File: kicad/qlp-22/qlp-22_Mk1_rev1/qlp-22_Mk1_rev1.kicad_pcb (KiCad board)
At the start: 2 copper layers, 301 x 153 mm, 51 parts

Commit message: Adds row connections and diode/switch labels
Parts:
- added L0: MountingHole_2.2mm_M2, MountingHole:MountingHole_2.2mm_M2, F.Cu at (84.0, 149.0)
- added L1: MountingHole_2.2mm_M2, MountingHole:MountingHole_2.2mm_M2, F.Cu at (164.3, 162.3)
- added L2: MountingHole_2.2mm_M2, MountingHole:MountingHole_2.2mm_M2, F.Cu at (181.7, 231.4)
- added R3: MountingHole_2.2mm_M2, MountingHole:MountingHole_2.2mm_M2, F.Cu at (208.7, 231.4)
- added R4: MountingHole_2.2mm_M2, MountingHole:MountingHole_2.2mm_M2, F.Cu at (226.1, 162.3)
- moved R5 40.5 mm to (306.4, 149.0), turned to 20 degrees
- moved D1:11 18.3 mm to (333.6, 165.2)
- moved S1:1 18.3 mm to (79.9, 160.3)
- moved S1:11 18.3 mm to (329.3, 153.4)
- moved D1:4 18.3 mm to (135.4, 183.1)
- moved D1:1 18.3 mm to (75.6, 172.0)
- moved S1:6 18.3 mm to (230.2, 173.5)
- moved D1:0 18.3 mm to (56.8, 165.2)
- moved D0:8 18.3 mm to (254.1, 122.3)
- moved S0:11 18.3 mm to (245.6, 215.8)
- moved S1:4 18.3 mm to (139.7, 171.4)
- moved S0:10 18.3 mm to (228.5, 227.4)
- moved D1:3 18.3 mm to (120.0, 166.9)
- moved D0:7 18.3 mm to (238.7, 138.5)
- moved S1:9 18.3 mm to (286.6, 153.0)
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- renumbered REF** to D0:0, REF** to D0:1, REF** to D0:10, REF** to D0:11, REF** to D0:2, REF** to D0:3, REF** to D0:4, REF** to D0:7, REF** to D0:8, REF** to D0:9, REF** to D1:0, REF** to D1:1, REF** to D1:10, REF** to D1:11, REF** to D1:2, REF** to D1:3, REF** to D1:4, REF** to D1:5, REF** to D1:6, REF** to D1:7, REF** to D1:8, REF** to D1:9, REF** to R5, REF** to RESET, REF** to S0:0, REF** to S0:1, REF** to S0:10, REF** to S0:11, REF** to S0:2, REF** to S0:3, REF** to S0:4, REF** to S0:7, REF** to S0:8, REF** to S0:9, REF** to S1:0, REF** to S1:1, REF** to S1:10, REF** to S1:11, REF** to S1:2, REF** to S1:3, REF** to S1:4, REF** to S1:5, REF** to S1:6, REF** to S1:7, REF** to S1:8, REF** to S1:9
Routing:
- net (no net): track 4237.9 -> 4507.6 mm
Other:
- outline, holes or cut-outs redrawn
- board text added: "OLED 128x64"
- board text added: "Raspberry Pi Pico"

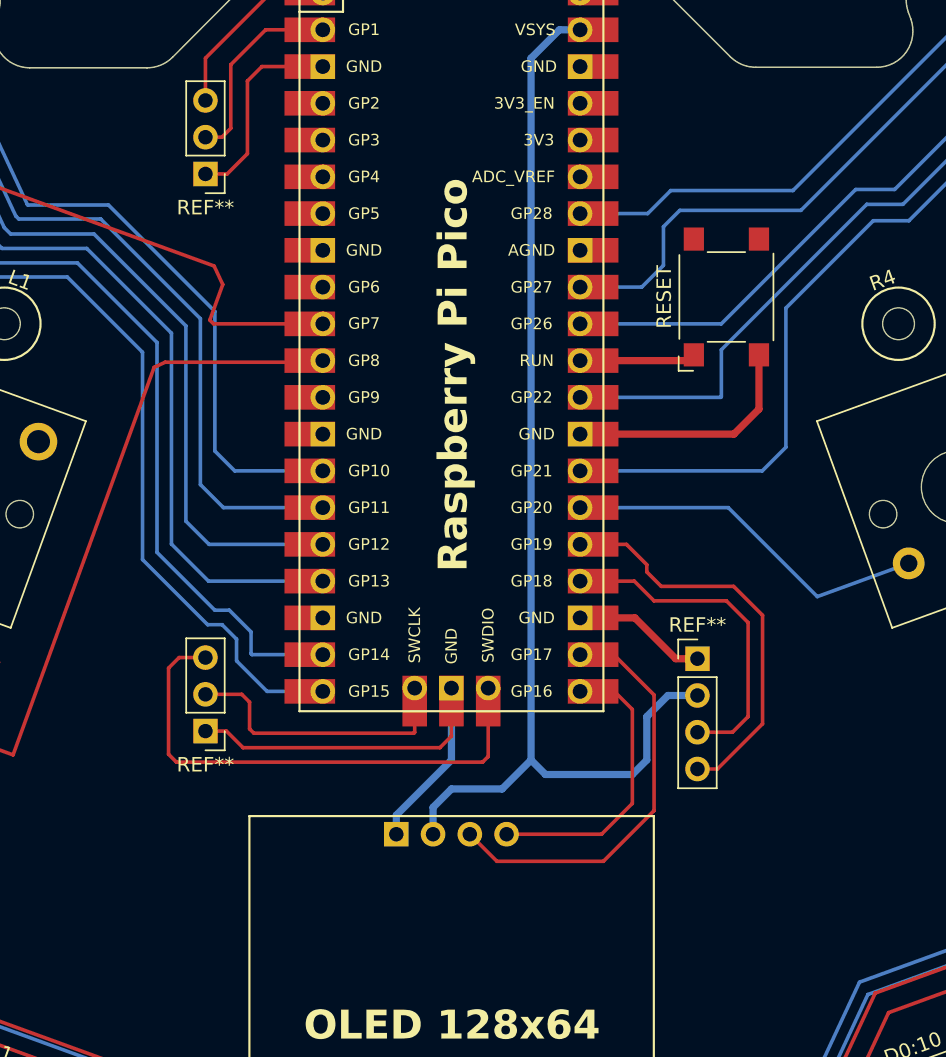
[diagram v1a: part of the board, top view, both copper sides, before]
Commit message: Adds pin labels for qlp-22_Mk1_rev1
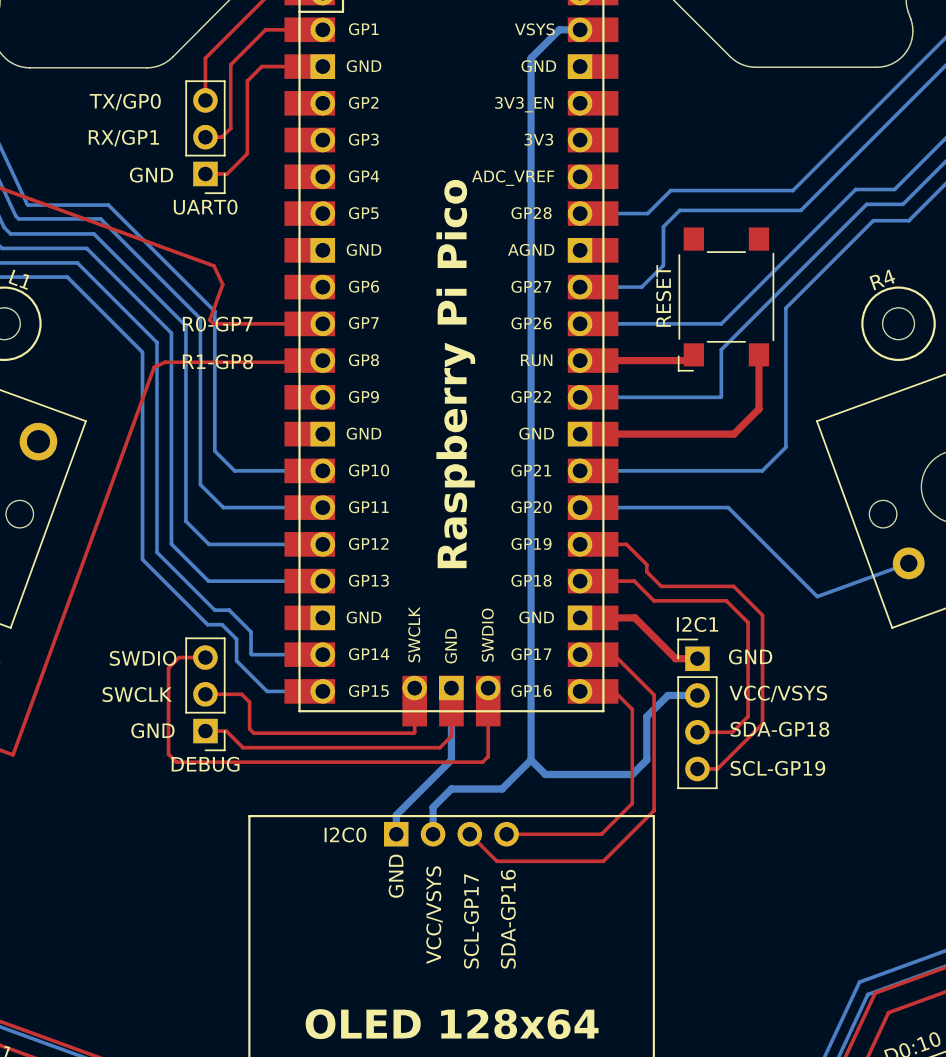
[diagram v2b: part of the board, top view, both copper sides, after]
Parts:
- renumbered REF** to DEBUG, REF** to I2C1, REF** to UART0
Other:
- board text added: "C0"
- board text added: "C1"
- board text added: "C10"
- board text added: "C11"
- board text added: "C2"
- board text added: "C3"
- board text added: "C4"
- board text added: "C5"
- board text added: "C6"
- board text added: "C7"
- board text added: "C8"
- board text added: "C9"
- board text added: "GND"
- board text added: "I2C0"
- board text added: "R0-GP7"
- board text added: "R1-GP8"
- board text added: "RX/GP1"
- board text added: "SCL-GP17"
- board text added: "SCL-GP19"
- board text added: "SDA-GP16"
- board text added: "SDA-GP18"
- board text added: "SWCLK"
- board text added: "SWDIO"
- board text added: "TX/GP0"
- board text added: "VCC/VSYS"
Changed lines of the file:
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@@
     (tags "Through hole pin header THT 1x04 2.54mm single row")
     (attr through_hole)
-    (fp_text reference "REF**" (at 0 -2.33) (layer "F.SilkS")
+    (fp_text reference "I2C1" (at 0 -2.33) (layer "F.SilkS")
         (effects (font (size 1 1) (thickness 0.15)))
     )
@@
     (tags "Through hole pin header THT 1x03 2.54mm single row")
     (attr through_hole)
-    (fp_text reference "REF**" (at 0 -2.33) (layer "F.SilkS")
+    (fp_text reference "UART0" (at 0 -2.33) (layer "F.SilkS")
         (effects (font (size 1 1) (thickness 0.15)))
     )
@@
     (tags "Through hole pin header THT 1x03 2.54mm single row")
     (attr through_hole)
-    (fp_text reference "REF**" (at 0 -2.33) (layer "F.SilkS")
+    (fp_text reference "DEBUG" (at 0 -2.33) (layer "F.SilkS")
         (effects (font (size 1 1) (thickness 0.15)))
     )
@@
   (gr_arc (start 86.208657 177.992821) (mid 84.915941 179.40347) (end 83.004371 179.486999)
     (stroke (width 0.1) (type default)) (layer "Edge.Cuts"))
+  (gr_text "C6" (at 209.1 175.6) (layer "B.SilkS")
+    (effects (font (size 1 1) (thickness 0.15)) (justify left bottom mirror))
+  )
+  (gr_text "C0" (at 183.7 173.1) (layer "B.SilkS")
+    (effects (font (size 1 1) (thickness 0.15)) (justify left bottom mirror))
+  )
+  (gr_text "C5" (at 183.7 188.2) (layer "B.SilkS")
+    (effects (font (size 1 1) (thickness 0.15)) (justify left bottom mirror))
+  )
+  (gr_text "C11" (at 209.9 155.2) (layer "B.SilkS")
+    (effects (font (size 1 1) (thickness 0.15)) (justify left bottom mirror))
+  )
+  (gr_text "C10" (at 210 160.5) (layer "B.SilkS")
+    (effects (font (size 1 1) (thickness 0.15)) (justify left bottom mirror))
+  )
+  (gr_text "C1" (at 183.7 175.6) (layer "B.SilkS")
+    (effects (font (size 1 1) (thickness 0.15)) (justify left bottom mirror))
+  )
+  (gr_text "C2" (at 183.7 178) (layer "B.SilkS")
+    (effects (font (size 1 1) (thickness 0.15)) (justify left bottom mirror))
+  )
+  (gr_text "C7" (at 209 173) (layer "B.SilkS")
+    (effects (font (size 1 1) (thickness 0.15)) (justify left bottom mirror))
+  )
+  (gr_text "C3" (at 183.7 180.5) (layer "B.SilkS")
+    (effects (font (size 1 1) (thickness 0.15)) (justify left bottom mirror))
+  )
+  (gr_text "C4" (at 183.7 185.7) (layer "B.SilkS")
+    (effects (font (size 1 1) (thickness 0.15)) (justify left bottom mirror))
+  )
+  (gr_text "C9" (at 209 162.8) (layer "B.SilkS")
+    (effects (font (size 1 1) (thickness 0.15)) (justify left bottom mirror))
+  )
+  (gr_text "C8" (at 209.1 167.9) (layer "B.SilkS")
+    (effects (font (size 1 1) (thickness 0.15)) (justify left bottom mirror))
+  )
+  (gr_text "VCC/VSYS" (at 214.4 188.4) (layer "F.SilkS")
+    (effects (font (size 1 1) (thickness 0.15)) (justify left bottom))
+  )
+  (gr_text "SWDIO" (at 171.5 186) (layer "F.SilkS")
+    (effects (font (size 1 1) (thickness 0.15)) (justify left bottom))
+  )
+  (gr_text "RX/GP1" (at 170 150) (layer "F.SilkS")
+    (effects (font (size 1 1) (thickness 0.15)) (justify left bottom))
+  )
+  (gr_text "R1-GP8" (at 176.5 165.5) (layer "F.SilkS")
+    (effects (font (size 1 1) (thickness 0.15)) (justify left bottom))
+  )
+  (gr_text "SCL-GP17" (at 197.2 206.9 90) (layer "F.SilkS")
+    (effects (font (size 1 1) (thickness 0.15)) (justify left bottom))
+  )
+  (gr_text "GND" (at 172.9 152.6) (layer "F.SilkS")
+    (effects (font (size 1 1) (thickness 0.15)) (justify left bottom))
+  )
+  (gr_text "SWCLK" (at 171 188.5) (layer "F.SilkS")
+    (effects (font (size 1 1) (thickness 0.15)) (justify left bottom))
+  )
   (gr_text "Raspberry Pi Pico" (at 196.487595 179.393895 90) (layer "F.SilkS")
     (effects (font (size 2 2) (thickness 0.3) bold) (justify left bottom))
   )
+  (gr_text "R0-GP7" (at 176.5 162.9) (layer "F.SilkS")
+    (effects (font (size 1 1) (thickness 0.15)) (justify left bottom))
+  )
+  (gr_text "VCC/VSYS" (at 194.6 206.5 90) (layer "F.SilkS")
+    (effects (font (size 1 1) (thickness 0.15)) (justify left bottom))
+  )
+  (gr_text "SDA-GP16" (at 199.75 206.9 90) (layer "F.SilkS")
+    (effects (font (size 1 1) (thickness 0.15)) (justify left bottom))
+  )
+  (gr_text "GND" (at 192 202 90) (layer "F.SilkS")
+    (effects (font (size 1 1) (thickness 0.15)) (justify left bottom))
+  )
   (gr_text "OLED 128x64" (at 184.987595 211.893897) (layer "F.SilkS")
     (effects (font (size 2 2) (thickness 0.3) bold) (justify left bottom))
   )
+  (gr_text "SDA-GP18" (at 214.4 190.9) (layer "F.SilkS")
+    (effects (font (size 1 1) (thickness 0.15)) (justify left bottom))
+  )
+  (gr_text "GND" (at 173 191) (layer "F.SilkS")
+    (effects (font (size 1 1) (thickness 0.15)) (justify left bottom))
+  )
+  (gr_text "GND" (at 214.3 185.9) (layer "F.SilkS")
+    (effects (font (size 1 1) (thickness 0.15)) (justify left bottom))
+  )
+  (gr_text "I2C0" (at 186.3 198.2) (layer "F.SilkS")
+    (effects (font (size 1 1) (thickness 0.15)) (justify left bottom))
+  )
+  (gr_text "SCL-GP19" (at 214.4 193.6) (layer "F.SilkS")
+    (effects (font (size 1 1) (thickness 0.15)) (justify left bottom))
+  )
+  (gr_text "TX/GP0" (at 170.2 147.5) (layer "F.SilkS")
+    (effects (font (size 1 1) (thickness 0.15)) (justify left bottom))
+  )
   (segment (start 248.491252 197.021995) (end 246.439129 191.383844) (width 0.25) (layer "F.Cu") (net 0))

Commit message: Finishes labeling for qlp-22_Mk1_rev1
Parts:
- moved S1:0 42.4 mm to (78.1, 114.5)
- moved D0:11 42.4 mm to (258.3, 165.2)
- moved R3 42.4 mm to (225.7, 192.5)
- moved S0:0 42.4 mm to (161.8, 176.9)
- moved S0:1 42.4 mm to (178.9, 188.5)
- moved I2C1 42.4 mm to (229.2, 146.5)
- moved R5 42.4 mm to (323.4, 110.1)
- moved S0:7 42.4 mm to (260.0, 111.4)
- moved S1:7 42.4 mm to (267.7, 132.5)
- moved D1:4 42.4 mm to (152.4, 144.3)
- moved S1:2 42.4 mm to (120.8, 114.1)
- moved D0:2 42.4 mm to (189.7, 195.1)
- moved D0:7 42.4 mm to (255.7, 99.6)
- moved D1:5 42.4 mm to (172.9, 146.4)
- moved REF** 42.4 mm to (212.2, 124.7)
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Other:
- board text added: "01-2024"
- board text added: "2024"
- board text added: "HAMLUND MFG."
- board text added: "JLCJLCJLCJLC"
- board text added: "Mk I"
- board text added: "QLP-22"
- board text added: "QLP-22-MK.1-REV.1"
- board text added: "Qwerty Linear Paginated Keyboard"
- board text added: "prototype revision 1"

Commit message: Adjusts qlp-22_Mk1_rev1 tracks around mounting holes
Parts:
- moved S0:3 6.07 mm to (148.0, 101.1)
- moved R4 6.07 mm to (242.1, 129.4)
- moved S1:2 6.07 mm to (119.8, 120.1)
- moved D1:7 6.07 mm to (271.0, 150.2)
- moved RESET 6.07 mm to (230.2, 127.5)
- moved D1:3 6.07 mm to (136.1, 134.0)
- moved D0:3 6.07 mm to (145.1, 86.8)
- moved DEBUG 6.07 mm to (194.2, 157.5)
- moved S1:6 6.07 mm to (246.2, 140.6)
- moved S0:2 6.07 mm to (191.6, 215.4)
- moved D0:10 6.07 mm to (240.2, 182.7)
- moved S0:1 6.07 mm to (177.9, 194.5)
- moved D0:2 6.07 mm to (188.7, 201.0)
- moved D0:8 6.07 mm to (270.1, 89.4)
- moved S1:9 6.07 mm to (302.6, 120.1)
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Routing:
- net (no net): track 4507.6 -> 4505.6 mm

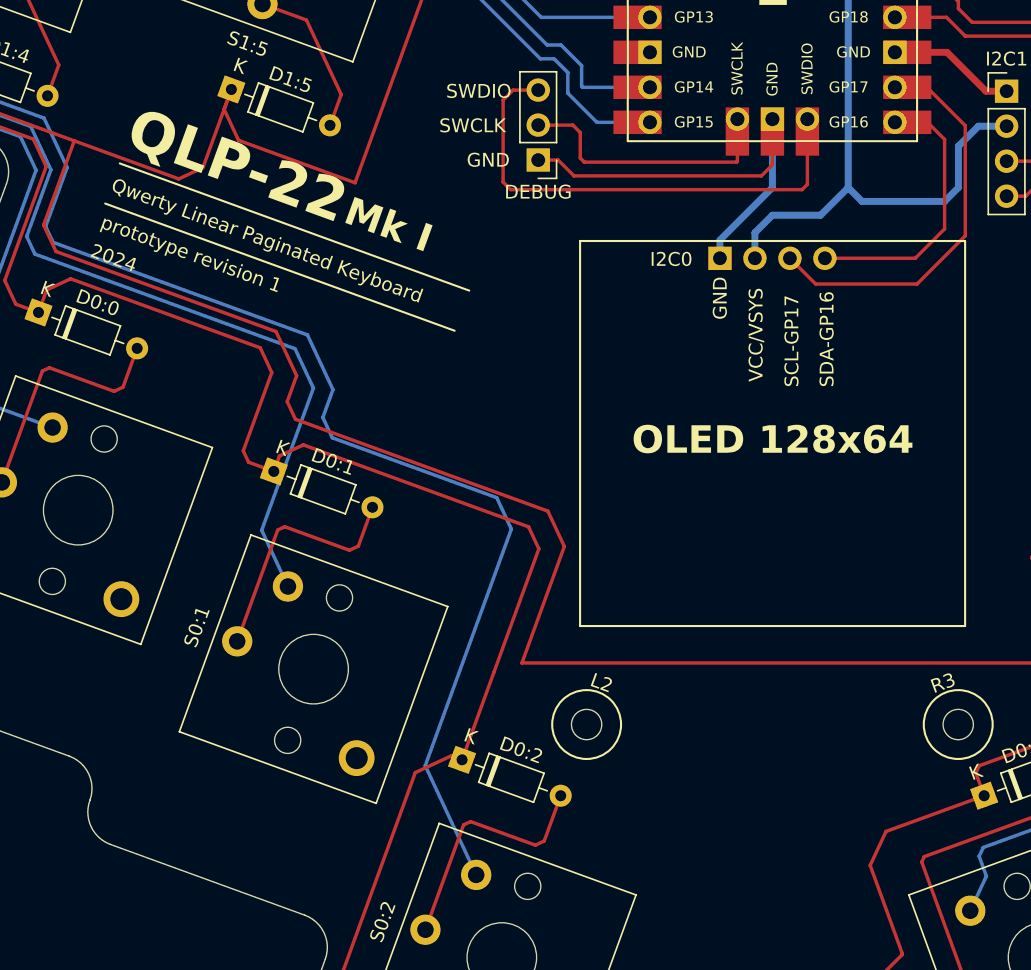
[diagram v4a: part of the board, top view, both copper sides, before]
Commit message: DRC and silkscreen updates
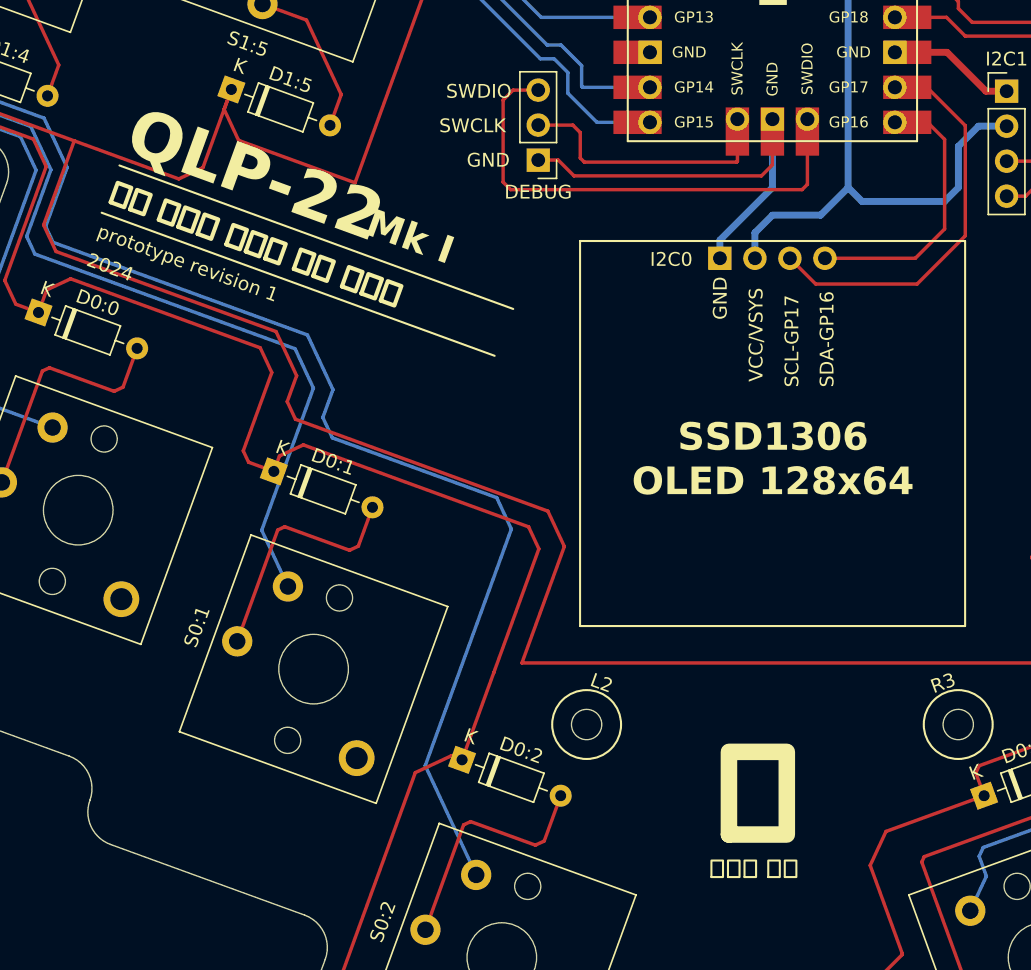
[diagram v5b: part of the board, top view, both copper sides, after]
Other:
- board text added: "SSD1306 OLED 128x64"
- board text added: "쿼티 리니어 페이지 매김 키보드"
- board text added: "햄"
- board text added: "햄룬드 제조"
- board text removed: "OLED 128x64"
- board text removed: "Qwerty Linear Paginated Keyboard"

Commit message: Final silkscreen and DRC tweaks before manufacturing
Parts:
- moved D0:9 9.97 mm to (228.9, 193.9)
- moved S0:7 9.97 mm to (261.3, 107.6)
- moved D0:2 9.97 mm to (191.0, 191.3)
- moved REF** 9.97 mm to (213.5, 154.9)
- moved D0:8 9.97 mm to (272.4, 79.7)
- moved D1:7 9.97 mm to (273.3, 140.5)
- moved S0:2 9.97 mm to (193.9, 205.7)
- moved S0:8 9.97 mm to (276.7, 91.4)
- moved D1:2 9.97 mm to (117.8, 122.2)
- moved REF** 9.97 mm to (213.5, 120.9)
- moved S1:4 9.97 mm to (158.0, 128.8)
- moved D1:10 9.97 mm to (333.1, 129.4)
- moved D0:0 9.97 mm to (160.2, 158.9)
- moved L2 9.97 mm to (200.0, 188.8)
- moved S0:9 9.97 mm to (233.1, 205.7)
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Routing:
- net (no net): track 4505.6 -> 4504.5 mm
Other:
- outline, holes or cut-outs redrawn
- board text added: "쿼티 리니어 페이지매김 키보드"
- board text removed: "쿼티 리니어 페이지 매김 키보드"
